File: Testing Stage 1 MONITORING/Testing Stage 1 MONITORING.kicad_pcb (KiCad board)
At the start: 2 copper layers, 86.6 x 116.8 mm, 78 parts, among them J1 Conn_01x06_Socket, J2 Conn_01x03_Pin, Q1 PMOS, Q2 NMOS, Q3 AO3401A, Q4 BUK7M67-60EX, Q5 BUK7M67-60EX, SW1 SW_Push, U1 BQ76920PW, U2 BQ78350DBT, U3 BQ76200PW

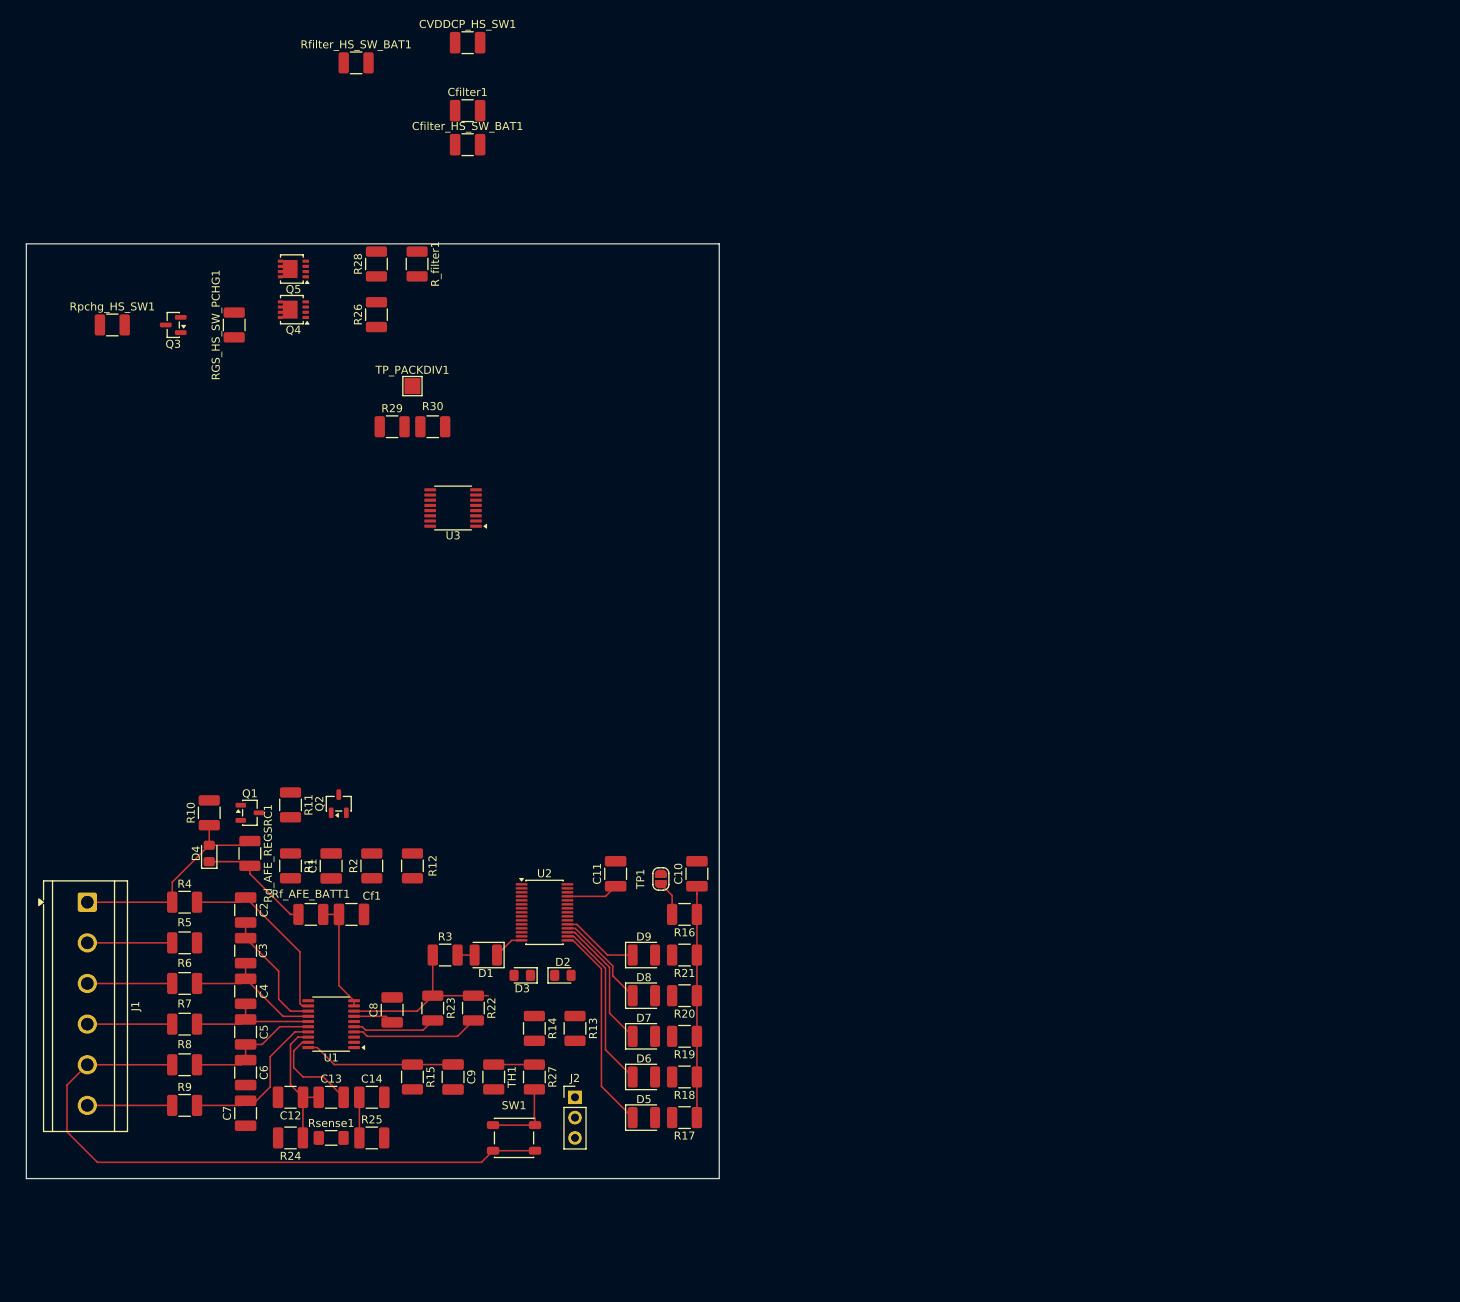
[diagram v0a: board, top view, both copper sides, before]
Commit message: need to fix high side control IC - no need for precharge system
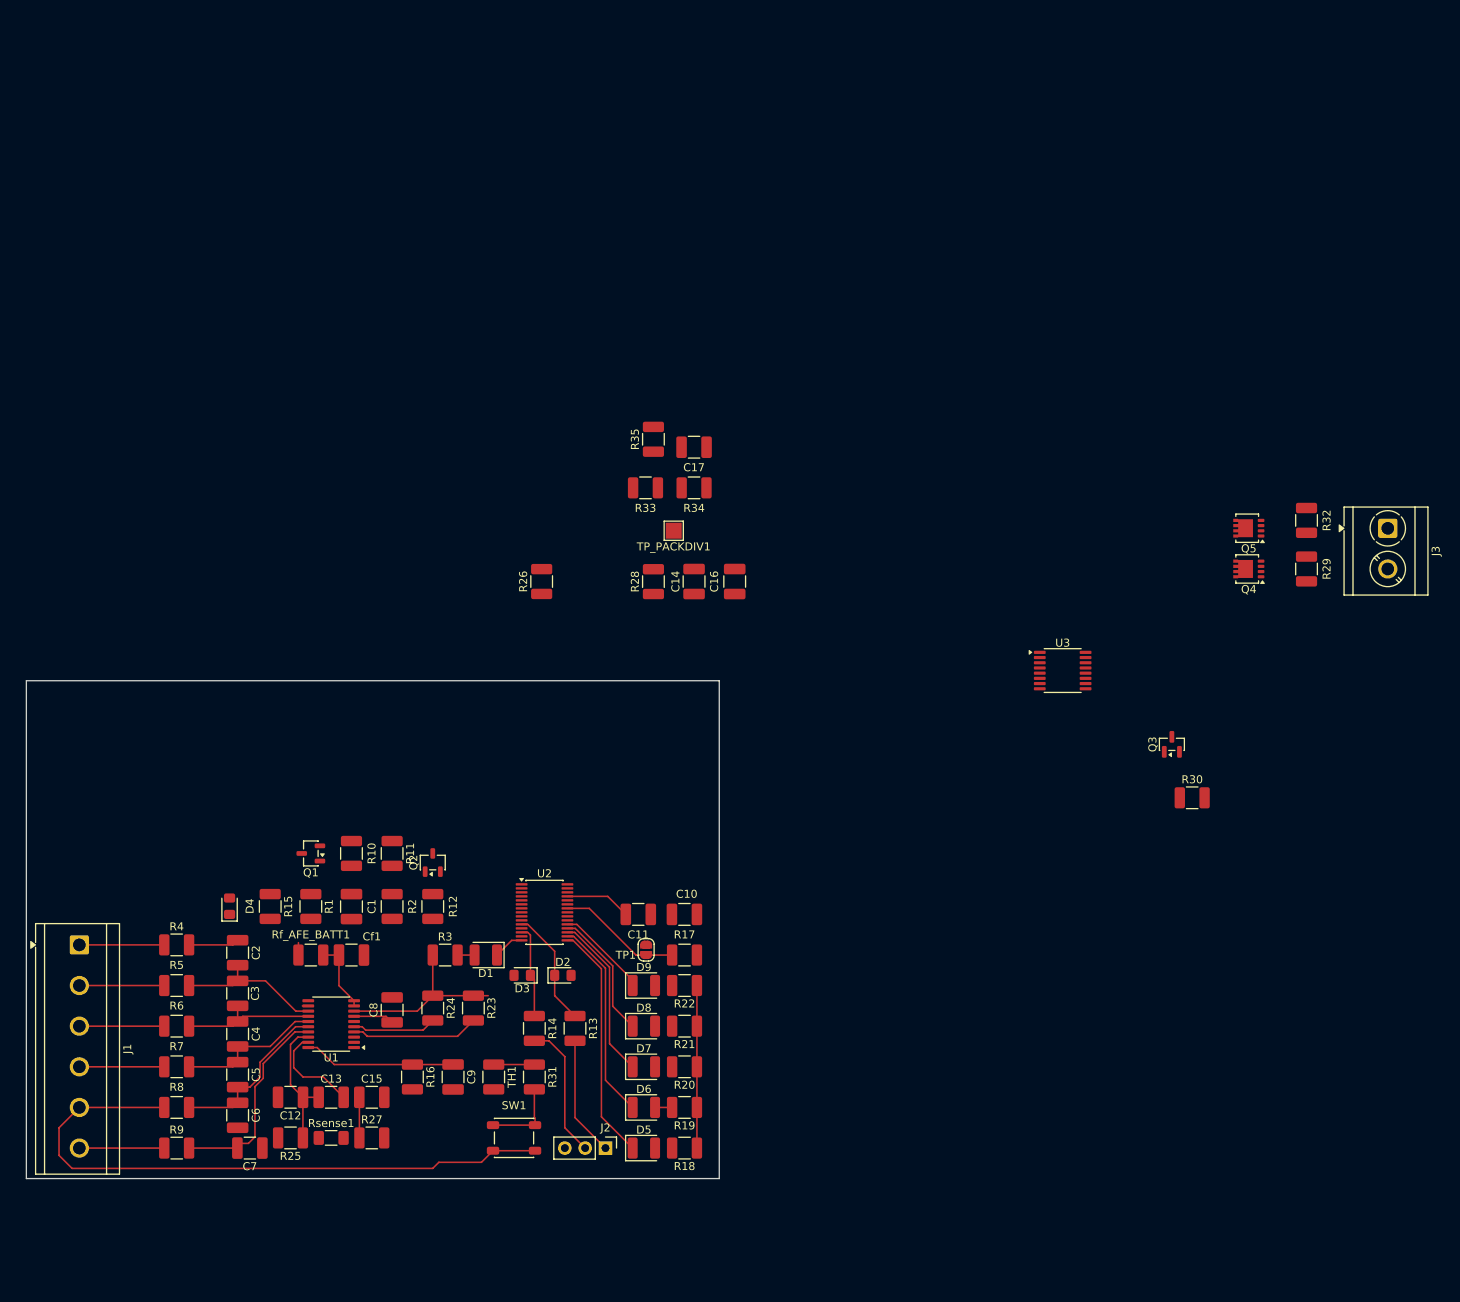
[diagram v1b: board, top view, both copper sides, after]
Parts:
- added J3: Conn_01x02, TerminalBlock_CUI:TerminalBlock_CUI_TB007-508-02_1x02_P5.08mm_Horizontal, F.Cu at (205.7, 61.0)
- moved Q3 135.4 mm to (178.8, 88.0), turned to 90 degrees
- moved R30 133.5 mm to (181.3, 94.6), turned to 0 degrees
- moved Q4 123.7 mm to (188.4, 66.0)
- moved Q5 123.7 mm to (188.4, 60.9)
- moved R32 120.6 mm to (195.6, 60.0)
- moved R29 120.5 mm to (195.6, 66.0)
- moved U3 78.9 mm to (165.1, 78.7), turned to 0 degrees
- moved C16 75.2 mm to (124.1, 67.6), turned to -90 degrees
- moved R28 74.7 mm to (113.9, 67.6), turned to 90 degrees
- moved R26 62.5 mm to (100.0, 67.6), turned to 90 degrees
- moved C14 61.5 mm to (119.0, 67.6), turned to 90 degrees
- moved C17 50.7 mm to (119.0, 50.8), turned to 180 degrees
- moved TP_PACKDIV1 37.3 mm to (116.5, 61.3), turned to 180 degrees
- moved R35 36.8 mm to (113.9, 49.8), turned to 90 degrees
- moved R34 33.5 mm to (119.0, 55.9)
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- renumbered Cfilter_HS_SW_BAT1 to C14, C14 to C15, CVDDCP_HS_SW1 to C16, Cfilter1 to C17, Rd_AFE_REGSRC1 to R15, R15 to R16, R16 to R17, R17 to R18, R18 to R19, R19 to R20, R20 to R21, R21 to R22, R22 to R23, R23 to R24, R24 to R25, Rpchg_HS_SW1 to R26, R25 to R27, Rfilter_HS_SW_BAT1 to R28, R26 to R29, RGS_HS_SW_PCHG1 to R30, R27 to R31, R28 to R32, R29 to R33, R30 to R34, R_filter1 to R35
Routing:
- net Net-(J2-Pin_2): track 0.00 -> 17.1 mm
- net /Top_cell_stack: track 27.5 -> 10.6 mm
- net Net-(U1-VC5): track 23.5 -> 7.05 mm
- net Net-(J2-Pin_1): track 0.00 -> 15.0 mm
- net /SMBD: track 0.00 -> 14.7 mm
- net Net-(D4-K): track 14.5 -> 1.55 mm
- net /SMBC: track 0.00 -> 11.6 mm
- net Net-(U2-~{MRST}): track 4.36 -> 15.5 mm
- net /VCC: track 51.6 -> 43.0 mm
- net Net-(U1-VC0): track 19.9 -> 25.7 mm
- net Net-(U1-VC1): track 17.0 -> 21.3 mm
- net /LED3: track 16.9 -> 20.7 mm
- net /LED4: track 12.4 -> 16.2 mm
- net /LED1: track 25.9 -> 29.8 mm
- net /LED2: track 21.4 -> 25.2 mm
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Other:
- board size 86.6 x 116.8 mm -> 86.6 x 62.2 mm

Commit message: fixed schematic, changed high side FETs, rough layout, still need to change footprints to 0805 so can be manufactured cheap at uni
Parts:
- removed Q3: AO3401A, Package_TO_SOT_SMD:SOT-23
- removed Q4: BUK7M67-60EX, Package_TO_SOT_SMD:LFPAK33
- removed the R30 at (181.3, 94.6)
- removed R34: 16k, Resistor_SMD:R_1210_3225Metric_Pad1.30x2.65mm_HandSolder
- removed R35: 100, Resistor_SMD:R_1210_3225Metric_Pad1.30x2.65mm_HandSolder
- added Q6: NMOS, Package_TO_SOT_THT:TO-220-3_Vertical, F.Cu at (53.3, 99.1)
- added R31: 300k, Resistor_SMD:R_1210_3225Metric_Pad1.30x2.65mm_HandSolder, F.Cu at (91.4, 95.2)
- C17: value 0.01u -> 10n
- Q5: value BUK7M67-60EX -> NMOS; footprint Package_TO_SOT_SMD:LFPAK33 -> Package_TO_SOT_THT:TO-220-3_Vertical
- R26: value 10M -> 100
- R28: value 100 -> 10M
- R32: value 10M -> 16k
- R33: value 300k -> 100
- moved Q5 147.6 mm to (45.7, 99.1)
- moved J3 139.5 mm to (68.6, 86.4), turned to 0 degrees
- moved R29 139.5 mm to (58.4, 91.4), turned to 180 degrees
- moved R32 111.4 mm to (91.4, 99.5), turned to 0 degrees
- moved R28 77.1 mm to (40.6, 91.4), turned to 0 degrees
- moved C14 75.7 mm to (45.7, 86.4), turned to 180 degrees
- moved C17 74.7 mm to (53.3, 86.4), turned to 0 degrees
- moved U3 66.3 mm to (101.6, 97.8), turned to 180 degrees
- moved R33 62.5 mm to (58.4, 86.4)
- moved R26 62.2 mm to (40.6, 86.4), turned to 0 degrees
- moved C16 51.7 mm to (81.3, 96.5), turned to 90 degrees
- moved TP_PACKDIV1 45.4 mm to (86.4, 95.2), turned to 0 degrees
- renumbered R31 to R30
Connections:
- Q5 pad 1: /PACK+ -> Net-(Q5-D)
- Q5 pad 2: /PACK+ -> /CHG_GATE
- Q5 pad 3: /PACK+ -> /Top_cell_stack
- R26 pad 2: Net-(Q3-D) -> Net-(U3-BAT)
- R28 pad 2: Net-(U3-BAT) -> /CHG_GATE
- R29 pad 1: Net-(Q4-S-Pad1) -> /PACK+
- R29 pad 2: /CHG_GATE -> /DSG_GATE
- R32 pad 1: /PACK+ -> /HS_SW_PACKDIV
- R32 pad 2: /DSG_GATE -> GND
- R33 pad 1: Net-(U3-PACKDIV) -> Net-(U3-PACK)
- R33 pad 2: /HS_SW_PACKDIV -> /PACK+
- U3 pad 14: /PCHG_GATE -> unconnected-(U3-PCHG-Pad14)
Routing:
- net /Top_cell_stack: track 10.6 -> 66.6 mm
- net /BAT: track 11.1 -> 42.1 mm
- net /PACK+: track 0.00 -> 13.3 mm
- net Net-(U1-VC5): track 7.05 -> 19.9 mm
- net Net-(D4-K): track 1.55 -> 11.3 mm
- net /CHG_GATE: track 0.00 -> 8.03 mm
- net /DSG_GATE: track 0.00 -> 8.03 mm
- net /HS_SW_PACKDIV: track 0.00 -> 7.74 mm
- net Net-(Q5-D): track 0.00 -> 7.62 mm
- net Net-(U3-PACKDIV): track 0.00 -> 6.13 mm
- net /VCC: track 43.0 -> 47.5 mm
- net Net-(Q2-D): track 0.00 -> 4.43 mm
- net /VEN: track 0.00 -> 3.20 mm
- net Net-(U3-BAT): track 0.00 -> 1.97 mm

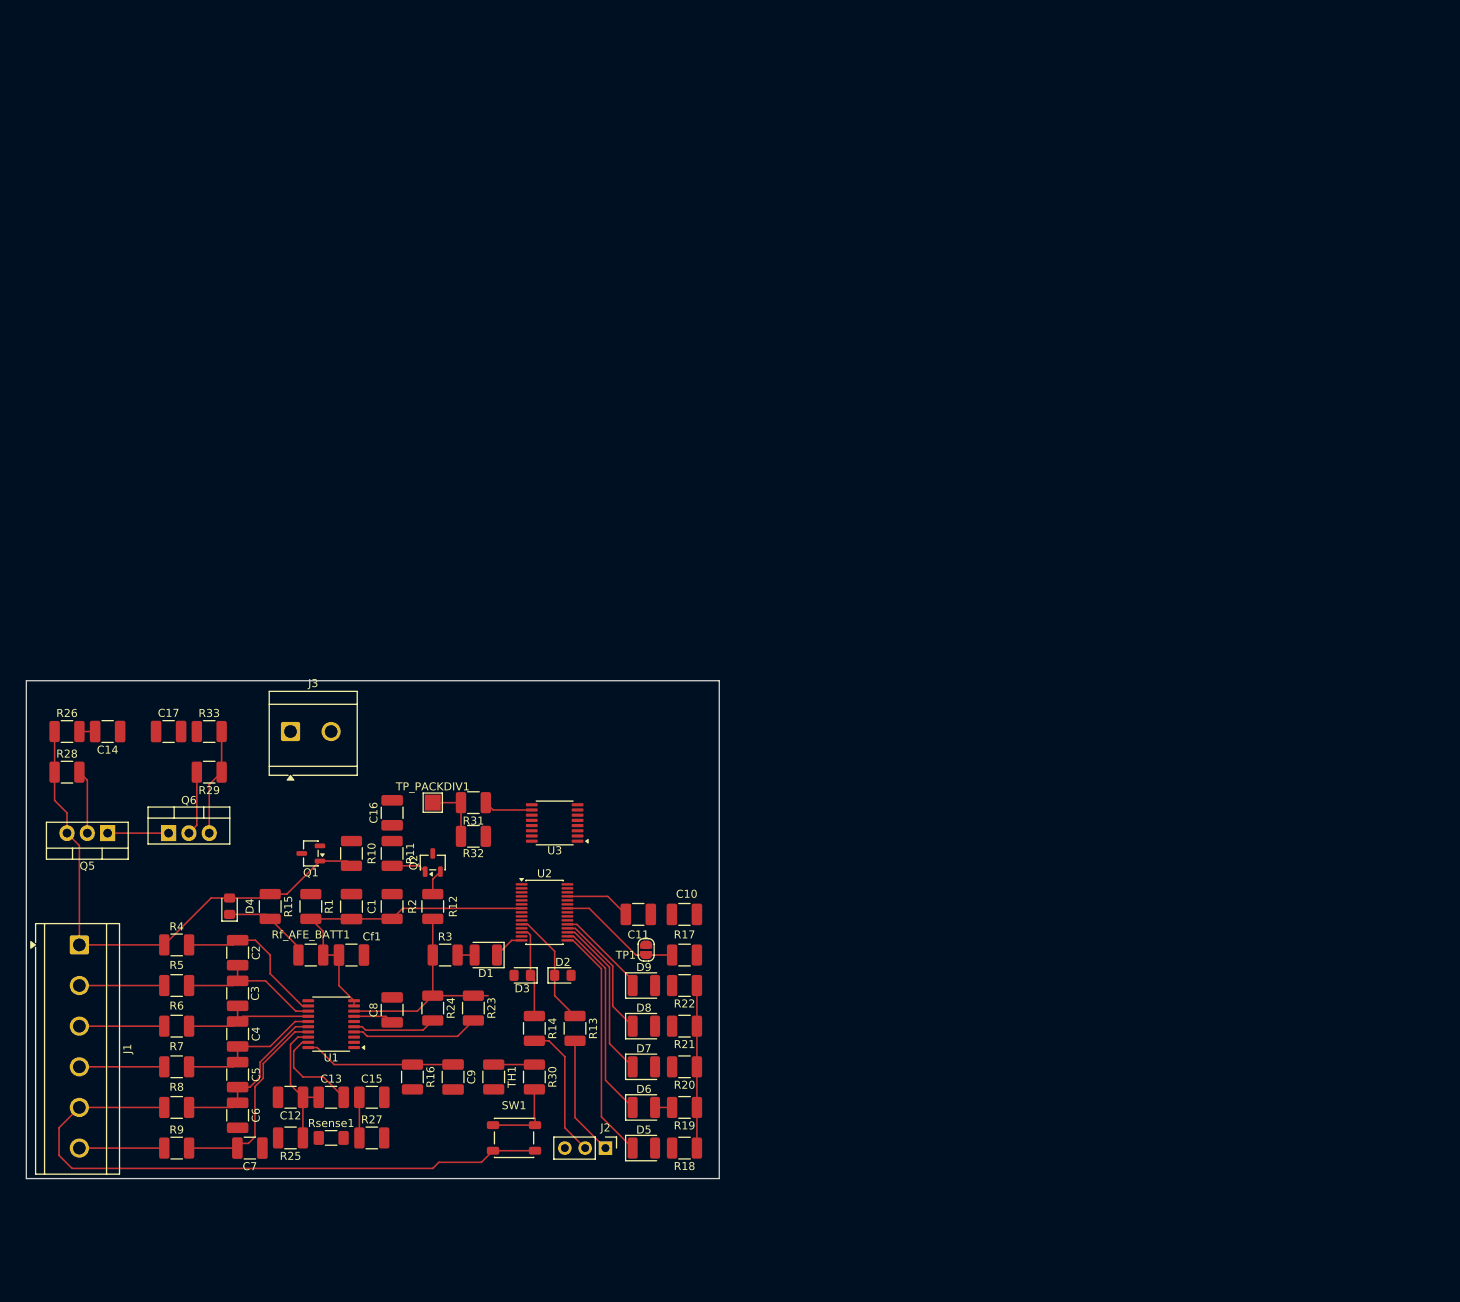
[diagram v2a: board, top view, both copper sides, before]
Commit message: routing and layout updates
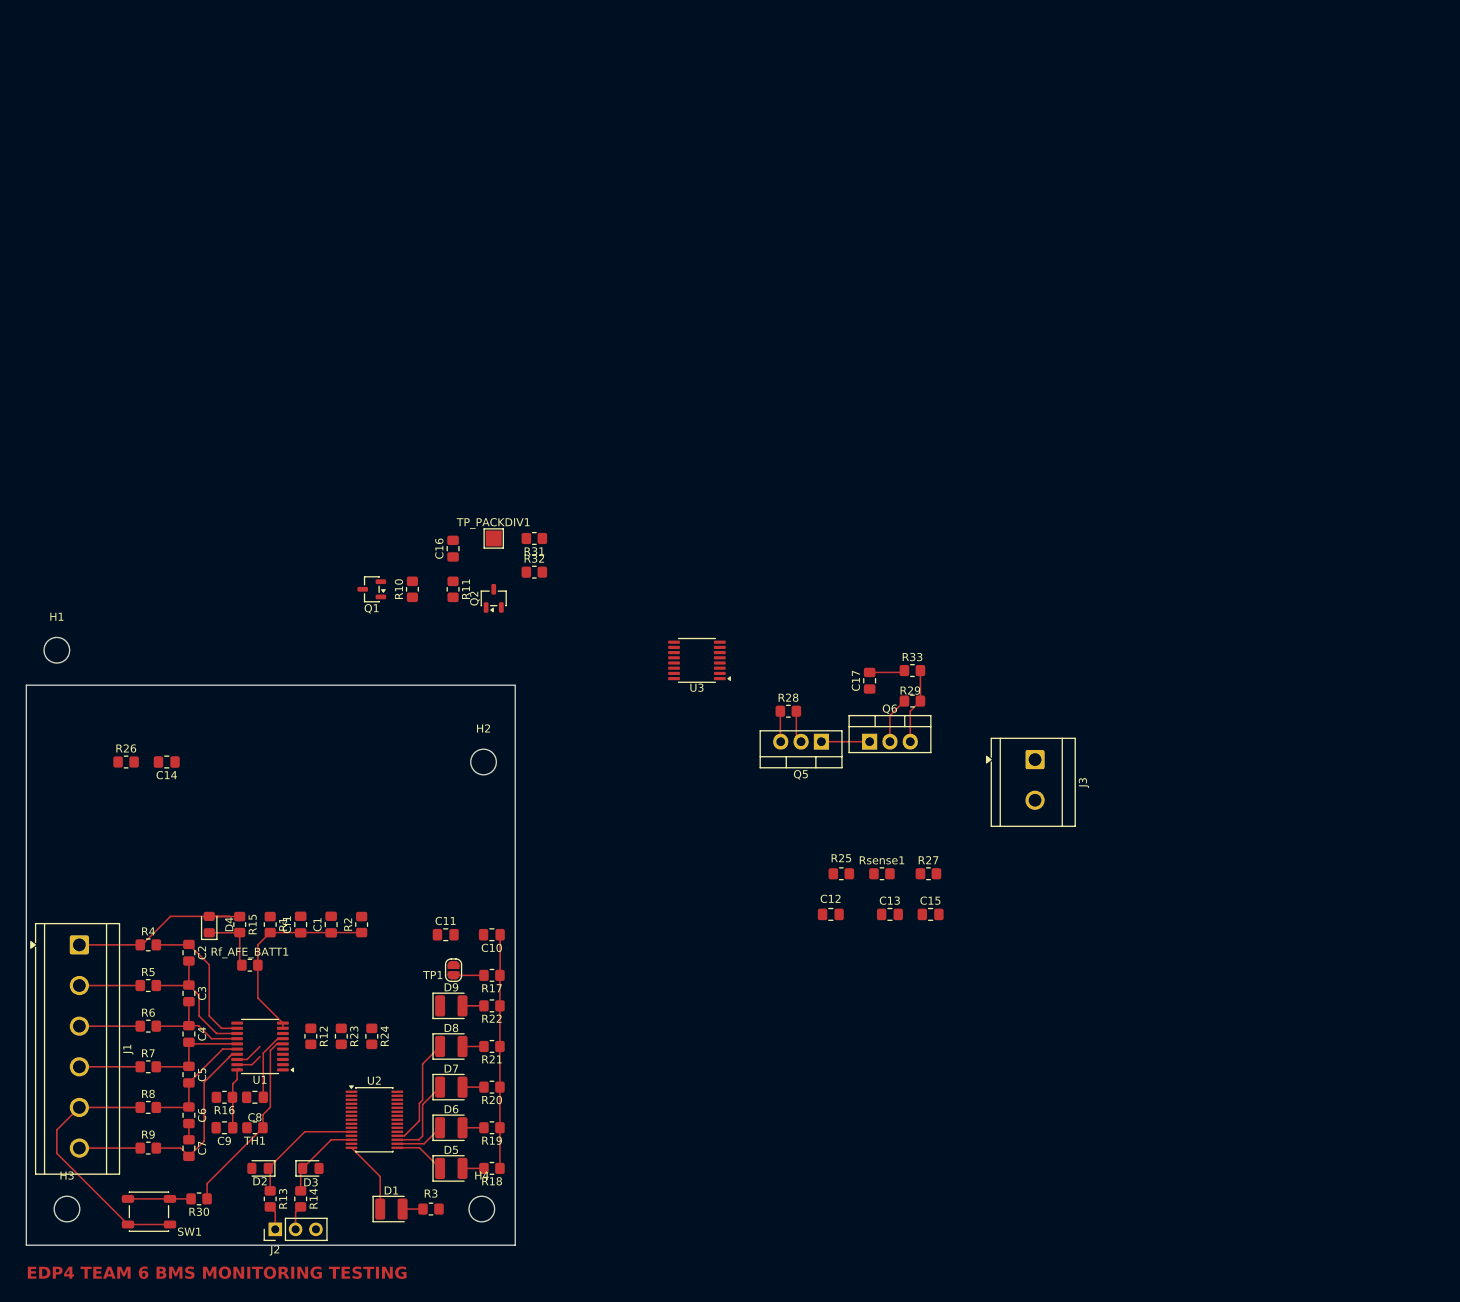
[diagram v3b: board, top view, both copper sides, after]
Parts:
- added H1: MountingHole, MountingHole:MountingHole_3.2mm_M3, F.Cu at (39.4, 76.2)
- added H2: MountingHole, MountingHole:MountingHole_3.2mm_M3, F.Cu at (92.7, 90.2)
- added H3: MountingHole, MountingHole:MountingHole_3.2mm_M3, F.Cu at (40.6, 146.1)
- added H4: MountingHole, MountingHole:MountingHole_3.2mm_M3, F.Cu at (92.5, 146.1)
- C1, C10, C11, C12, C13, C14, C15, C16, C17, C2, C3, C4, C5, C6, C7, C8, C9, Cf1: footprint Capacitor_SMD:C_1210_3225Metric_Pad1.33x2.70mm_HandSolder -> Capacitor_SMD:C_0805_2012Metric_Pad1.18x1.45mm_HandSolder
- R1, R10, R11, R12, R13, R14, R15, R16, R17, R18, R19, R2, R20, R21, R22, R23, R24, R25, R26, R27, R28, R29, R3, R30, R31, R32, R33, R4, R5, R6, R7, R8, R9, Rf_AFE_BATT1, TH1: footprint Resistor_SMD:R_1210_3225Metric_Pad1.30x2.65mm_HandSolder -> Resistor_SMD:R_0805_2012Metric_Pad1.20x1.40mm_HandSolder
- Rsense1: footprint Resistor_SMD:R_1206_3216Metric_Pad1.30x1.75mm_HandSolder -> Resistor_SMD:R_0805_2012Metric_Pad1.20x1.40mm_HandSolder
- moved J3 93.1 mm to (161.6, 89.9), turned to -90 degrees
- moved R28 90.5 mm to (130.8, 83.8)
- moved Q5 89.9 mm to (134.9, 87.6)
- moved Q6 88.4 mm to (141.0, 87.6)
- moved R29 88.3 mm to (146.3, 82.5)
- moved R33 88.2 mm to (146.3, 78.7)
- moved C17 87.9 mm to (141.0, 80.0), turned to 90 degrees
- moved R27 77.0 mm to (148.3, 104.1)
- moved R25 76.4 mm to (137.4, 104.1)
- moved Rsense1 76.4 mm to (142.5, 104.1)
- moved C15 73.5 mm to (148.6, 109.2)
- moved C13 73.5 mm to (143.5, 109.2)
- moved C12 71.3 mm to (136.1, 109.2)
- moved SW1 46.6 mm to (50.9, 146.4)
- moved D2 44.9 mm to (64.8, 141.0), turned to 180 degrees
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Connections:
- J3 pad 2: GND -> /PACK-
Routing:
- net /Cell_one: track 78.7 -> 32.8 mm
- net /Top_cell_stack: track 66.6 -> 27.9 mm
- net /LED1: track 29.8 -> 6.42 mm
- net /LED2: track 25.2 -> 6.18 mm
- net /TS1_AFE: track 5.08 -> 23.7 mm
- net /VCC: track 47.5 -> 29.2 mm
- net /BAT: track 42.1 -> 25.3 mm
- net /SDA_AFE: track 16.0 -> 0.00 mm
- net Net-(J2-Pin_2): track 17.1 -> 3.07 mm
- net /SRN: track 17.2 -> 3.28 mm
- net /SRP: track 16.9 -> 3.54 mm
- net Net-(J2-Pin_1): track 15.0 -> 3.07 mm
- net /LED5: track 11.7 -> 0.00 mm
- net Net-(U2-~{MRST}): track 15.5 -> 3.80 mm
- net /ALERT_AFE: track 19.0 -> 8.21 mm
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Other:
- board size 86.6 x 62.2 mm -> 61.1 x 70 mm
- board text added: "EDP4 TEAM 6 BMS MONITORING TESTING"
- board text removed: "${REFERENCE}"
